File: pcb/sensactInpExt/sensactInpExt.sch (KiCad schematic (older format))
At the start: 61 parts, among them P1 CONN_02X06, P2 CONN_02X05, P3 CONN_02X16, U1 SRV05, U2 SRV05, U3 SRV05, U4 SRV05

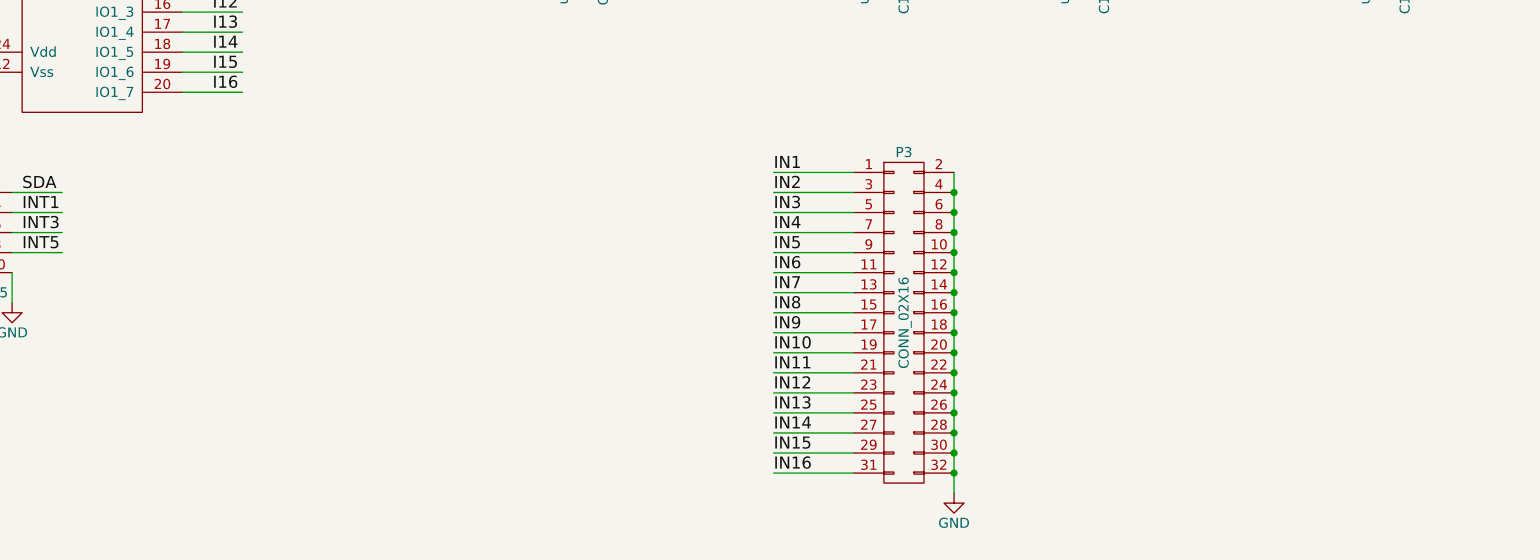
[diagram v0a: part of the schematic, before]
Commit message: sensactPWMExt as ordered
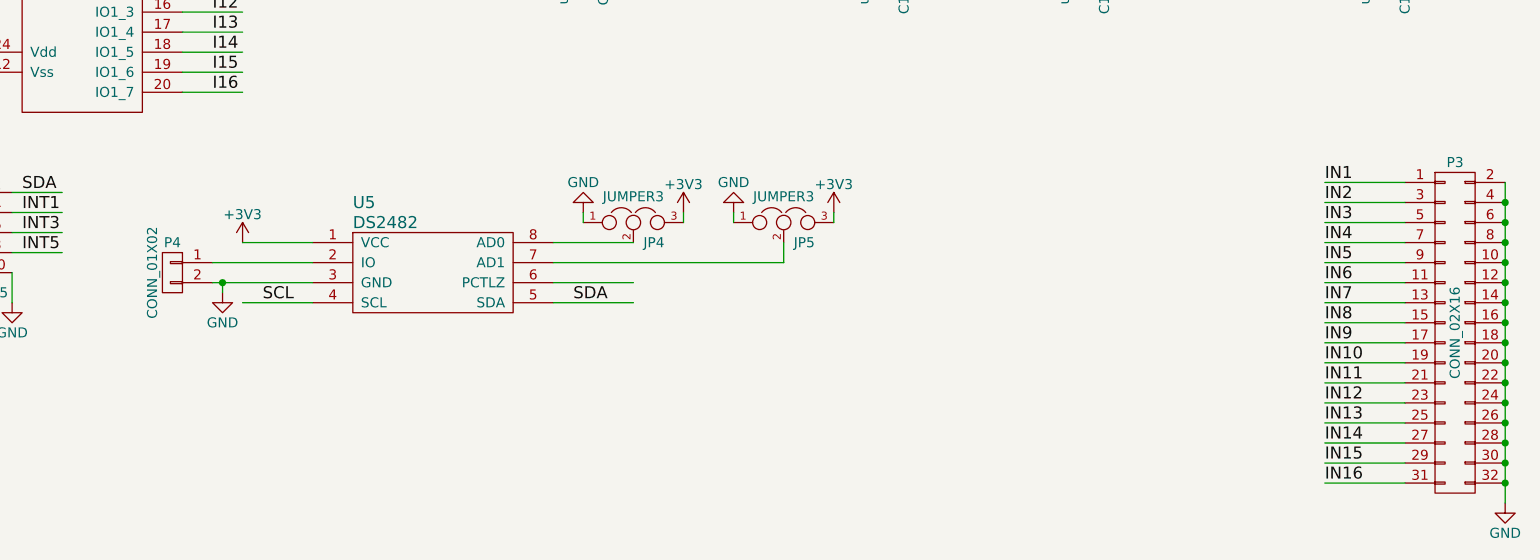
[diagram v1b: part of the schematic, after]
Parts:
- added JP4, JP5: JUMPER3, symbol JUMPER3
- added P4: CONN_01X02, symbol CONN_01X02
- added U5: DS2482, symbol DS2482
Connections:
- wire segments 166 -> 180
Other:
- moved on the sheet: P3

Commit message: SensactInpExt
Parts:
- added C19: u1, Capacitors_SMD:C_0805_HandSoldering, symbol C
- JP4, JP5: footprint (none) -> sensact:SMD-solder-bridge-3pin
- P4: footprint (none) -> sensact:KF141R-2p
- U5: footprint (none) -> sensact:SOIC-8_3.9x4.9mm_Pitch1.27mm_handsolder
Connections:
- wire segments 180 -> 185
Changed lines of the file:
@@
 	7700 1500 8000 1500
 Text Label 5750 1200 0    60   ~ 0
+IN2
+Text Label 5750 1500 0    60   ~ 0
 IN1
-Text Label 5750 1500 0    60   ~ 0
-IN2
 Text Label 7850 1500 0    60   ~ 0
+IN4
+Text Label 7850 1200 0    60   ~ 0
 IN3
-Text Label 7850 1200 0    60   ~ 0
-IN4
 Connection ~ 6300 850
 Connection ~ 7400 850
@@
 Connection ~ 7400 1850
 Text Label 6500 850  0    60   ~ 0
+I2
+Text Label 6500 1850 0    60   ~ 0
 I1
-Text Label 6500 1850 0    60   ~ 0
-I2
 Text Label 7050 1850 0    60   ~ 0
+I4
+Text Label 7050 850  0    60   ~ 0
 I3
-Text Label 7050 850  0    60   ~ 0
-I4
 $Comp
 L SRV05 U2
@@
 	7700 3000 8000 3000
 Text Label 5750 2700 0    60   ~ 0
+IN6
+Text Label 5750 3000 0    60   ~ 0
 IN5
-Text Label 5750 3000 0    60   ~ 0
-IN6
 Text Label 7850 3000 0    60   ~ 0
+IN8
+Text Label 7850 2700 0    60   ~ 0
 IN7
-Text Label 7850 2700 0    60   ~ 0
-IN8
 Connection ~ 6300 2350
 Connection ~ 7400 2350
@@
 Connection ~ 7400 3350
 Text Label 6500 2350 0    60   ~ 0
+I6
+Text Label 6500 3350 0    60   ~ 0
 I5
-Text Label 6500 3350 0    60   ~ 0
-I6
 Text Label 7050 3350 0    60   ~ 0
+I8
+Text Label 7050 2350 0    60   ~ 0
 I7
-Text Label 7050 2350 0    60   ~ 0
-I8
 $Comp
 L SRV05 U3
@@
 	10200 1500 10500 1500
 Text Label 8250 1200 0    60   ~ 0
+IN10
+Text Label 8250 1500 0    60   ~ 0
 IN9
-Text Label 8250 1500 0    60   ~ 0
-IN10
 Text Label 10350 1500 0    60   ~ 0
+IN12
+Text Label 10350 1200 0    60   ~ 0
 IN11
-Text Label 10350 1200 0    60   ~ 0
-IN12
 Connection ~ 8800 850
 Connection ~ 9900 850
@@
 Connection ~ 9900 1850
 Text Label 9000 850  0    60   ~ 0
+I10
+Text Label 9000 1850 0    60   ~ 0
 I9
-Text Label 9000 1850 0    60   ~ 0
-I10
 Text Label 9550 1850 0    60   ~ 0
+I12
+Text Label 9550 850  0    60   ~ 0
 I11
-Text Label 9550 850  0    60   ~ 0
-I12
 $Comp
 L SRV05 U4
@@
 	10200 3000 10500 3000
 Text Label 8250 2700 0    60   ~ 0
+IN14
+Text Label 8250 3000 0    60   ~ 0
 IN13
-Text Label 8250 3000 0    60   ~ 0
-IN14
 Text Label 10350 3000 0    60   ~ 0
+IN16
+Text Label 10350 2700 0    60   ~ 0
 IN15
-Text Label 10350 2700 0    60   ~ 0
-IN16
 Connection ~ 8800 2350
 Connection ~ 9900 2350
@@
 Connection ~ 9900 3350
 Text Label 9000 2350 0    60   ~ 0
+I14
+Text Label 9000 3350 0    60   ~ 0
 I13
-Text Label 9000 3350 0    60   ~ 0
-I14
 Text Label 9550 3350 0    60   ~ 0
+I16
+Text Label 9550 2350 0    60   ~ 0
 I15
-Text Label 9550 2350 0    60   ~ 0
-I16
 $Comp
 L JUMPER3 JP1
@@
 	2750 4800 2500 4800
 Text Label 3300 4400 0    60   ~ 0
+SCL
+Text Label 2500 4500 0    60   ~ 0
 SDA
-Text Label 2500 4500 0    60   ~ 0
-SCL
 Text Label 3300 4500 0    60   ~ 0
 INT1
@@
 F 3 "" H 2400 800 50  0000 C CNN
 	1    2400 2000
-	1    0    0    -1
+	-1   0    0    -1
 $EndComp
 Wire Wire Line
@@
 $EndComp
 Wire Wire Line
-	950  1000 1200 1000
+	950  1000 1700 1000
 Wire Wire Line
 	1200 1000 1200 1100
@@
 	1200 1500 1200 1400
 Wire Wire Line
-	950  1500 1200 1500
-Wire Wire Line
-	950  1400 950  1500
+	950  1500 1450 1500
+Wire Wire Line
+	950  1400 950  3800
 Connection ~ 1100 1500
 $Comp
@@
 F 0 "U5" H 4950 5150 60  0000 L CNN
 F 1 "DS2482" H 4950 5050 60  0000 L CNN
-F 2 "" H 5350 4800 60  0000 C CNN
+F 2 "sensact:SOIC-8_3.9x4.9mm_Pitch1.27mm_handsolder" H 5350 4800 60  0001 C CNN
 F 3 "" H 5350 4800 60  0000 C CNN
 	1    5350 4800
@@
 F 0 "JP4" H 6400 4450 50  0000 L CNN
 F 1 "JUMPER3" H 6350 4650 50  0000 C BNN
-F 2 "" H 6350 4550 50  0000 C CNN
+F 2 "sensact:SMD-solder-bridge-3pin" H 6350 4550 50  0001 C CNN
 F 3 "" H 6350 4550 50  0000 C CNN
 	1    6350 4550
@@
 F 0 "JP5" H 7150 4450 50  0000 L CNN
 F 1 "JUMPER3" H 7100 4650 50  0000 C BNN
-F 2 "" H 7100 4550 50  0000 C CNN
+F 2 "sensact:SMD-solder-bridge-3pin" H 7100 4550 50  0001 C CNN
 F 3 "" H 7100 4550 50  0000 C CNN
 	1    7100 4550
@@
 F 0 "P4" H 4050 4950 50  0000 C CNN
 F 1 "CONN_01X02" V 4150 4800 50  0000 C CNN
-F 2 "" H 4050 4800 50  0000 C CNN
+F 2 "sensact:KF141R-2p" H 4050 4800 50  0001 C CNN
 F 3 "" H 4050 4800 50  0000 C CNN
 	1    4050 4800
-	-1   0    0    -1
+	-1   0    0    1
 $EndComp
 Wire Wire Line
 	4300 4850 4300 4900
 Connection ~ 4300 4850
+$Comp
+L C C19
+U 1 1 57E7094E
+P 1450 1250
+F 0 "C19" H 1475 1350 50  0000 L CNN
+F 1 "u1" H 1475 1150 50  0000 L CNN
+F 2 "Capacitors_SMD:C_0805_HandSoldering" H 1488 1100 50  0001 C CNN
+F 3 "" H 1450 1250 50  0000 C CNN
+	1    1450 1250
+	1    0    0    -1
+$EndComp
+Wire Wire Line
+	1450 1000 1450 1100
+Connection ~ 1200 1000
+Wire Wire Line
+	1450 1500 1450 1400
+Connection ~ 1200 1500
+Wire Wire Line
+	3100 3700 1700 3700
+Wire Wire Line
+	1700 3700 1700 1000
+Connection ~ 1450 1000
+Wire Wire Line
+	950  3800 3100 3800
+Connection ~ 950  1500
 $EndSCHEMATC

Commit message: Redesign sensactInpExt
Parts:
- removed P1: CONN_02X06, Pin_Headers:Pin_Header_Straight_2x06, symbol CONN_02X06
- added JP6: INT1, sensact:SMD-solder-bridge, symbol JUMPER
- added JP7: INT2, sensact:SMD-solder-bridge, symbol JUMPER
- added JP8: INT3, sensact:SMD-solder-bridge, symbol JUMPER
- JP1: value JUMPER3 -> A2
- JP2: value JUMPER3 -> A1
- JP3: value JUMPER3 -> A0
- JP4: value JUMPER3 -> AD0
- JP5: value JUMPER3 -> AD1
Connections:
- net labels added: +24V
- net labels removed: INT4, INT5, INT6
- wire segments 185 -> 182
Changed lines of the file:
@@
 P 2550 2650
 F 0 "JP1" H 2600 2550 50  0000 L CNN
-F 1 "JUMPER3" H 2550 2750 50  0000 C BNN
+F 1 "A2" H 2550 2750 50  0000 C BNN
 F 2 "sensact:SMD-solder-bridge-3pin" H 2550 2650 50  0001 C CNN
 F 3 "" H 2550 2650 50  0000 C CNN
@@
 P 2550 3000
 F 0 "JP2" H 2600 2900 50  0000 L CNN
-F 1 "JUMPER3" H 2550 3100 50  0000 C BNN
+F 1 "A1" H 2550 3100 50  0000 C BNN
 F 2 "sensact:SMD-solder-bridge-3pin" H 2550 3000 50  0001 C CNN
 F 3 "" H 2550 3000 50  0000 C CNN
@@
 P 2550 3350
 F 0 "JP3" H 2600 3250 50  0000 L CNN
-F 1 "JUMPER3" H 2550 3450 50  0000 C BNN
+F 1 "A0" H 2550 3450 50  0000 C BNN
 F 2 "sensact:SMD-solder-bridge-3pin" H 2550 3350 50  0001 C CNN
 F 3 "" H 2550 3350 50  0000 C CNN
@@
 L GND #PWR033
 U 1 1 57C8DA1F
-P 3250 4950
-F 0 "#PWR033" H 3250 4700 50  0001 C CNN
-F 1 "GND" H 3250 4800 50  0000 C CNN
-F 2 "" H 3250 4950 50  0000 C CNN
-F 3 "" H 3250 4950 50  0000 C CNN
-	1    3250 4950
-	1    0    0    -1
-$EndComp
-Wire Wire Line
-	3250 4800 3250 4950
+P 3250 4800
+F 0 "#PWR033" H 3250 4550 50  0001 C CNN
+F 1 "GND" H 3250 4650 50  0000 C CNN
+F 2 "" H 3250 4800 50  0000 C CNN
+F 3 "" H 3250 4800 50  0000 C CNN
+	1    3250 4800
+	1    0    0    -1
+$EndComp
 Wire Wire Line
 	3250 4400 3500 4400
@@
 	3250 4600 3500 4600
 Wire Wire Line
-	3250 4700 3500 4700
-Wire Wire Line
 	2750 4600 2500 4600
-Wire Wire Line
-	2750 4700 2500 4700
-Wire Wire Line
-	2750 4800 2500 4800
 Text Label 3300 4400 0    60   ~ 0
 SCL
@@
 Text Label 3300 4600 0    60   ~ 0
 INT3
-Text Label 2500 4700 0    60   ~ 0
-INT4
-Text Label 3300 4700 0    60   ~ 0
-INT5
-Text Label 2500 4800 0    60   ~ 0
-INT6
 Wire Wire Line
 	3100 2300 2850 2300
@@
 Wire Wire Line
 	2700 2450 2700 1750
-$Comp
-L CONN_02X06 P1
-U 1 1 57C8F73E
-P 2400 2000
-F 0 "P1" H 2400 2350 50  0000 C CNN
-F 1 "CONN_02X06" H 2400 1650 50  0000 C CNN
-F 2 "Pin_Headers:Pin_Header_Straight_2x06" H 2400 800 50  0001 C CNN
-F 3 "" H 2400 800 50  0000 C CNN
-	1    2400 2000
-	-1   0    0    -1
-$EndComp
 Wire Wire Line
 	2700 2250 2650 2250
@@
 Connection ~ 2700 1850
 Wire Wire Line
-	2150 1750 1850 1750
-Wire Wire Line
-	2150 1850 1850 1850
-Wire Wire Line
-	2150 1950 1850 1950
-Wire Wire Line
-	2150 2050 1850 2050
-Wire Wire Line
-	2150 2150 1850 2150
-Wire Wire Line
-	2150 2250 1850 2250
-Text Label 1850 1750 0    60   ~ 0
+	2050 1750 1750 1750
+Wire Wire Line
+	2050 1850 1750 1850
+Wire Wire Line
+	2050 1950 1750 1950
+Text Label 1750 1750 0    60   ~ 0
 INT1
-Text Label 1850 1850 0    60   ~ 0
+Text Label 1750 1850 0    60   ~ 0
 INT2
-Text Label 1850 1950 0    60   ~ 0
+Text Label 1750 1950 0    60   ~ 0
 INT3
-Text Label 1850 2050 0    60   ~ 0
-INT4
-Text Label 1850 2150 0    60   ~ 0
-INT5
-Text Label 1850 2250 0    60   ~ 0
-INT6
 $Comp
 L GND #PWR034
@@
 $EndComp
 Wire Wire Line
-	950  1000 1700 1000
+	950  1000 1450 1000
+Wire Wire Line
+	1450 1000 1550 1050
 Wire Wire Line
 	1200 1000 1200 1100
@@
 P 6350 4550
 F 0 "JP4" H 6400 4450 50  0000 L CNN
-F 1 "JUMPER3" H 6350 4650 50  0000 C BNN
+F 1 "AD0" H 6350 4650 50  0000 C BNN
 F 2 "sensact:SMD-solder-bridge-3pin" H 6350 4550 50  0001 C CNN
 F 3 "" H 6350 4550 50  0000 C CNN
@@
 P 7100 4550
 F 0 "JP5" H 7150 4450 50  0000 L CNN
-F 1 "JUMPER3" H 7100 4650 50  0000 C BNN
+F 1 "AD1" H 7100 4650 50  0000 C BNN
 F 2 "sensact:SMD-solder-bridge-3pin" H 7100 4550 50  0001 C CNN
 F 3 "" H 7100 4550 50  0000 C CNN
@@
 Connection ~ 1200 1500
 Wire Wire Line
-	3100 3700 1700 3700
-Wire Wire Line
-	1700 3700 1700 1000
+	3100 3700 1550 3750
+Wire Wire Line
+	1550 3750 1550 1050
 Connection ~ 1450 1000
 Wire Wire Line
 	950  3800 3100 3800
 Connection ~ 950  1500
+$Comp
+L +24V #PWR042
+U 1 1 584729A8
+P 2500 4700
+F 0 "#PWR042" H 2500 4550 50  0001 C CNN
+F 1 "+24V" H 2500 4840 50  0000 C CNN
+F 2 "" H 2500 4700 50  0000 C CNN
+F 3 "" H 2500 4700 50  0000 C CNN
+	1    2500 4700
+	0    -1   -1   0
+$EndComp
+$Comp
+L +24V #PWR043
+U 1 1 58472A3E
+P 3500 4700
+F 0 "#PWR043" H 3500 4550 50  0001 C CNN
+F 1 "+24V" H 3500 4840 50  0000 C CNN
+F 2 "" H 3500 4700 50  0000 C CNN
+F 3 "" H 3500 4700 50  0000 C CNN
+	1    3500 4700
+	0    1    1    0
+$EndComp
+Wire Wire Line
+	3500 4700 3250 4700
+Wire Wire Line
+	2750 4700 2500 4700
+$Comp
+L GND #PWR044
+U 1 1 58473327
+P 2650 4800
+F 0 "#PWR044" H 2650 4550 50  0001 C CNN
+F 1 "GND" H 2650 4650 50  0000 C CNN
+F 2 "" H 2650 4800 50  0000 C CNN
+F 3 "" H 2650 4800 50  0000 C CNN
+	1    2650 4800
+	1    0    0    -1
+$EndComp
+Wire Wire Line
+	2750 4800 2650 4800
+$Comp
+L JUMPER JP6
+U 1 1 58488370
+P 2350 1750
+F 0 "JP6" H 2350 1900 50  0000 C CNN
+F 1 "INT1" H 2350 1670 50  0000 C CNN
+F 2 "sensact:SMD-solder-bridge" H 2350 1750 50  0001 C CNN
+F 3 "" H 2350 1750 50  0000 C CNN
+	1    2350 1750
+	1    0    0    -1
+$EndComp
+$Comp
+L JUMPER JP7
+U 1 1 584886A8
+P 2350 1850
+F 0 "JP7" H 2350 2000 50  0000 C CNN
+F 1 "INT2" H 2350 1770 50  0000 C CNN
+F 2 "sensact:SMD-solder-bridge" H 2350 1850 50  0001 C CNN
+F 3 "" H 2350 1850 50  0000 C CNN
+	1    2350 1850
+	1    0    0    -1
+$EndComp
+$Comp
+L JUMPER JP8
+U 1 1 58488749
+P 2350 1950
+F 0 "JP8" H 2350 2100 50  0000 C CNN
+F 1 "INT3" H 2350 1870 50  0000 C CNN
+F 2 "sensact:SMD-solder-bridge" H 2350 1950 50  0001 C CNN
+F 3 "" H 2350 1950 50  0000 C CNN
+	1    2350 1950
+	1    0    0    -1
+$EndComp
 $EndSCHEMATC

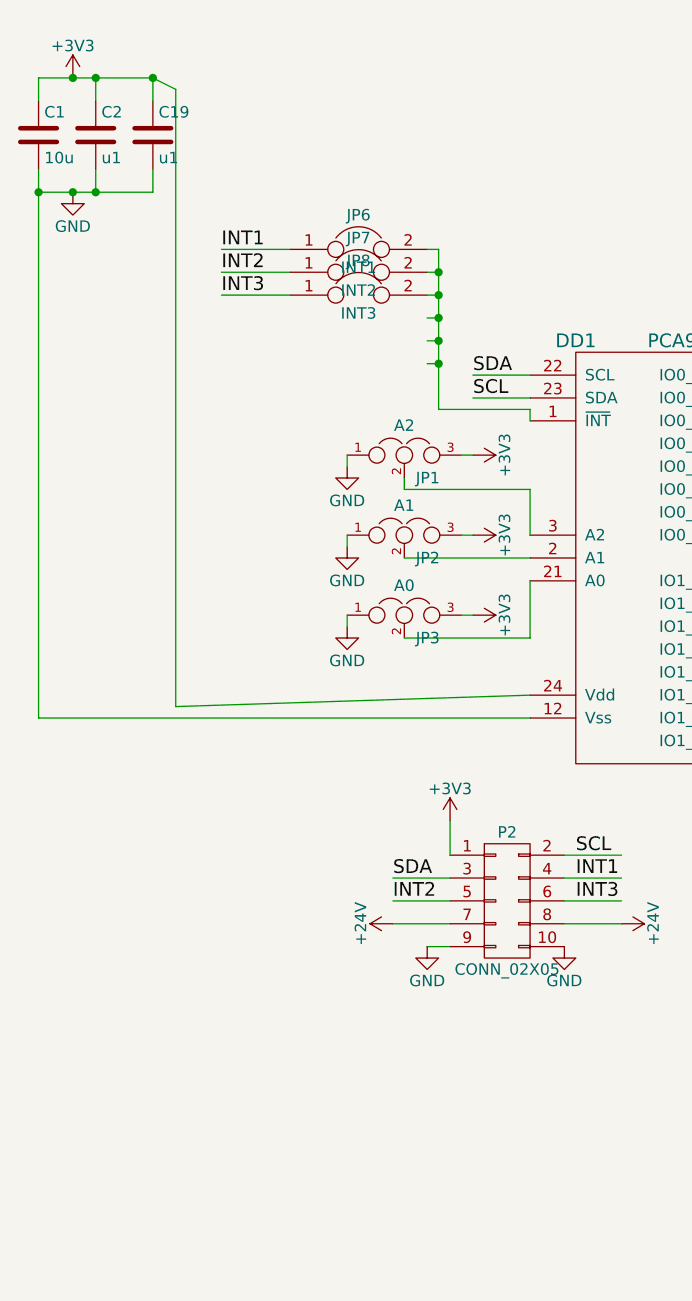
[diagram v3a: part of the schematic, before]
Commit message: Finalize Extension Modules PCB order
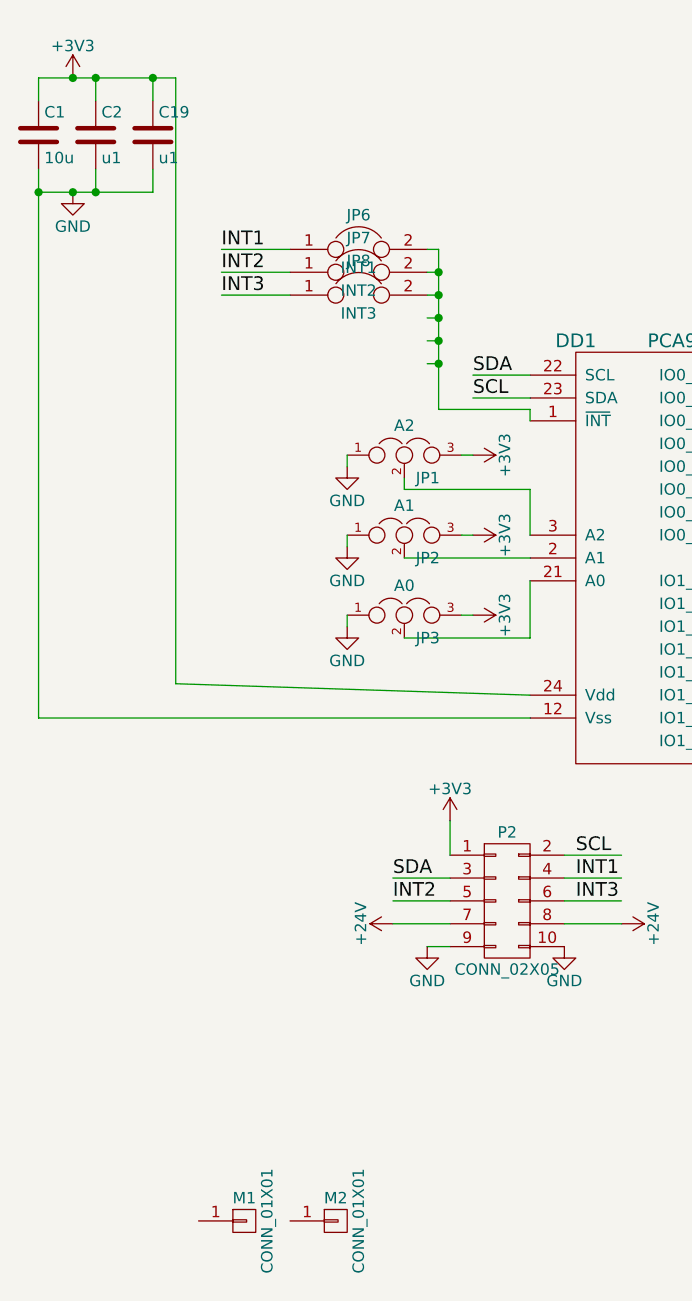
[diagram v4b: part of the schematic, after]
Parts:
- added M1, M2: CONN_01X01, Mounting_Holes:MountingHole_4.3mm_M4_DIN965, symbol CONN_01X01
- P3: footprint Pin_Headers:Pin_Header_Angled_2x16 -> w_conn_strip:vasch_strip_16x2
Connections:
- wire segments 182 -> 181
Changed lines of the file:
@@
 F 0 "P3" H 10450 5950 50  0000 C CNN
 F 1 "CONN_02X16" V 10450 5100 50  0000 C CNN
-F 2 "Pin_Headers:Pin_Header_Angled_2x16" H 10450 4000 50  0001 C CNN
+F 2 "w_conn_strip:vasch_strip_16x2" H 10450 4000 50  0001 C CNN
 F 3 "" H 10450 4000 50  0000 C CNN
 	1    10450 5100
@@
 $EndComp
 Wire Wire Line
-	950  1000 1450 1000
-Wire Wire Line
-	1450 1000 1550 1050
+	950  1000 1550 1000
 Wire Wire Line
 	1200 1000 1200 1100
@@
 Connection ~ 1200 1500
 Wire Wire Line
-	3100 3700 1550 3750
-Wire Wire Line
-	1550 3750 1550 1050
+	3100 3700 1550 3650
+Wire Wire Line
+	1550 3650 1550 1000
 Connection ~ 1450 1000
 Wire Wire Line
@@
 	1    0    0    -1
 $EndComp
+$Comp
+L CONN_01X01 M1
+U 1 1 585B1950
+P 1850 6000
+F 0 "M1" H 1850 6100 50  0000 C CNN
+F 1 "CONN_01X01" V 1950 6000 50  0000 C CNN
+F 2 "Mounting_Holes:MountingHole_4.3mm_M4_DIN965" H 1850 6000 50  0001 C CNN
+F 3 "" H 1850 6000 50  0000 C CNN
+	1    1850 6000
+	1    0    0    -1
+$EndComp
+$Comp
+L CONN_01X01 M2
+U 1 1 585B1A70
+P 2250 6000
+F 0 "M2" H 2250 6100 50  0000 C CNN
+F 1 "CONN_01X01" V 2350 6000 50  0000 C CNN
+F 2 "Mounting_Holes:MountingHole_4.3mm_M4_DIN965" H 2250 6000 50  0001 C CNN
+F 3 "" H 2250 6000 50  0000 C CNN
+	1    2250 6000
+	1    0    0    -1
+$EndComp

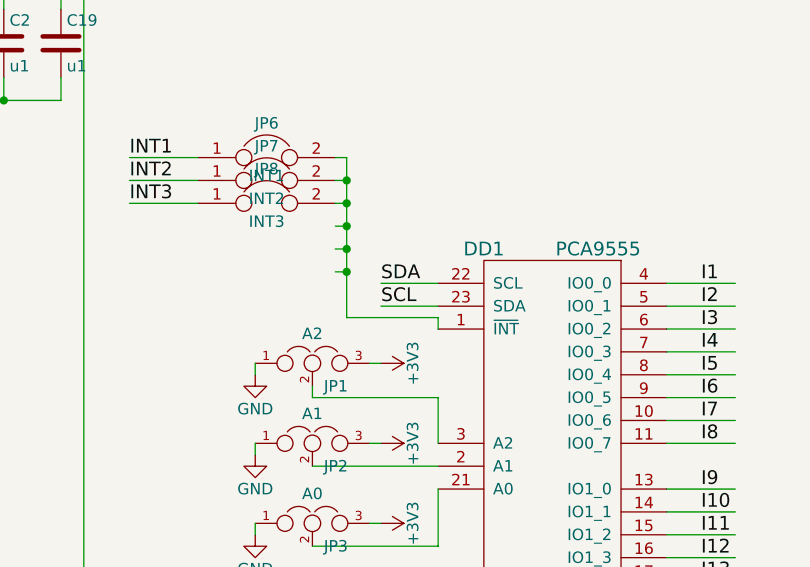
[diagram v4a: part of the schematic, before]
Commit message: Added BusDriver
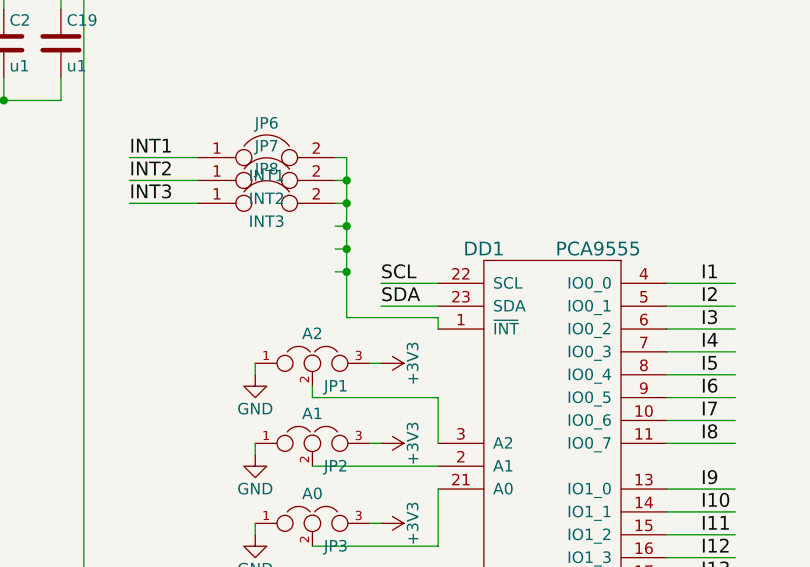
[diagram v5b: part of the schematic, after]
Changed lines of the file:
@@
 	3100 2400 2850 2400
 Text Label 2850 2300 0    60   ~ 0
+SCL
+Text Label 2850 2400 0    60   ~ 0
 SDA
-Text Label 2850 2400 0    60   ~ 0
-SCL
 Wire Wire Line
 	3100 2500 3100 2450
